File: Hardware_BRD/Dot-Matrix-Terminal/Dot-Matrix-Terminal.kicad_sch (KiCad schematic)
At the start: 61 parts, among them J1 USB_B, J2 Conn_01x17, J3 Conn_01x10, J4 Conn_01x02, J5 Barrel_Jack, J6 Conn_01x02, J7 Conn_01x02, J8 Conn_01x02, Q1 IRLML0030, Q10 IRLML0030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

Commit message: unsuccessful attempt at single layer routing
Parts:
- removed R22: 10k, Resistor_SMD:R_0603_1608Metric_Pad0.98x0.95mm_HandSolder, symbol Device:R
- added R23, R24, R25, R27: 10k, Resistor_SMD:R_0603_1608Metric_Pad0.98x0.95mm_HandSolder, symbol Device:R
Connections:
- net +24V: now also J7.1 (Pin_1), J7.2 (Pin_2); no longer J4.1 (Pin_1), J4.2 (Pin_2)
- net +3.3V: now also J4.1 (Pin_1), J4.2 (Pin_2), R15.2, R23.1, R24.2, R25.1, R27.1; no longer J7.1 (Pin_1), J7.2 (Pin_2), R15.1
- net FEED_L_SNS: now also U1.28 (IO17), R23.2; no longer U1.16 (IO13)
- net FEED_R: now also U1.24 (IO2); no longer Q11.1 (G), R11.1, U1.28 (IO17), U1.30 (IO18)
- net FEED_R_SNS: now also U1.30 (IO18), R24.1; no longer U1.13 (IO14)
- net FINE_SNS: now also R27.2
- net LINE_SNS: now also U1.27 (IO16), R25.2; no longer U1.14 (IO12)
- net PIN1: now also U1.16 (IO13); no longer U1.31 (IO19)
- net PIN3: now also U1.14 (IO12); no longer U1.24 (IO2)
- net PIN5: now also U1.13 (IO14); no longer U1.27 (IO16)
- net at Q15.3 (C), SW2.2, U1.25 (IO0): now also R15.1; no longer R15.2
- net INDEX_SNS: no longer names the net of J3.6 (Pin_6)
- net INDEX_SNS: no longer U1.23 (IO15)
- new net FEED_L: Q11.1 (G), R11.1, U1.23 (IO15)
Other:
- moved on the sheet: D1, D2, D3, D4, D5, D6, J4, J7, Q1, Q10, Q11, Q12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

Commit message: MVP board
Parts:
- removed R23, R24, R25, R27: 10k, Resistor_SMD:R_0603_1608Metric_Pad0.98x0.95mm_HandSolder, symbol Device:R
- added C7, C8: 1000u, Capacitor_THT:C_Radial_D16.0mm_H25.0mm_P7.50mm, symbol Device:C
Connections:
- net +24V: now also J6.1 (Pin_1), J6.2 (Pin_2), C7.1, C8.1; no longer J7.1 (Pin_1), J7.2 (Pin_2)
- net +3.3V: now also J8.1 (Pin_1), J8.2 (Pin_2); no longer J4.1 (Pin_1), J4.2 (Pin_2)
- net FEED_L: now also U1.26 (IO4); no longer U1.23 (IO15)
- net FEED_R: now also U1.27 (IO16); no longer U1.24 (IO2)
- net FINE_SNS: now also U1.28 (IO17); no longer U1.26 (IO4)
- net GND: now also J4.1 (Pin_1), J4.2 (Pin_2), J7.1 (Pin_1), J7.2 (Pin_2), C7.2, C8.2; no longer J6.1 (Pin_1), J6.2 (Pin_2), J8.1 (Pin_1), J8.2 (Pin_2)
- net LINE_SNS: now also U1.30 (IO18); no longer U1.27 (IO16)
- net MOTOR: now also U1.8 (IO32); no longer U1.6 (IO34)
- net PIN1: now also U1.24 (IO2); no longer U1.16 (IO13)
- net PIN2: now also U1.12 (IO27); no longer U1.10 (IO25)
- net PIN3: now also U1.23 (IO15); no longer U1.14 (IO12)
- net PIN4: now also U1.13 (IO14); no longer U1.11 (IO26)
- net PIN5: now also U1.16 (IO13); no longer U1.13 (IO14)
- net PIN6: now also U1.10 (IO25); no longer U1.8 (IO32)
- net PIN7: now also U1.14 (IO12); no longer U1.12 (IO27)
- net PIN8: now also U1.9 (IO33); no longer U1.7 (IO35)
- net PIN9: now also U1.11 (IO26); no longer U1.9 (IO33)
- net FEED_L_SNS: no longer names the net of J3.9 (Pin_9)
- net FEED_L_SNS: no longer U1.28 (IO17)
- net FEED_R_SNS: no longer names the net of J3.10 (Pin_10)
- net FEED_R_SNS: no longer U1.30 (IO18)
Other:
- moved on the sheet: J3, J4, J6, J7, J8, R13, R14

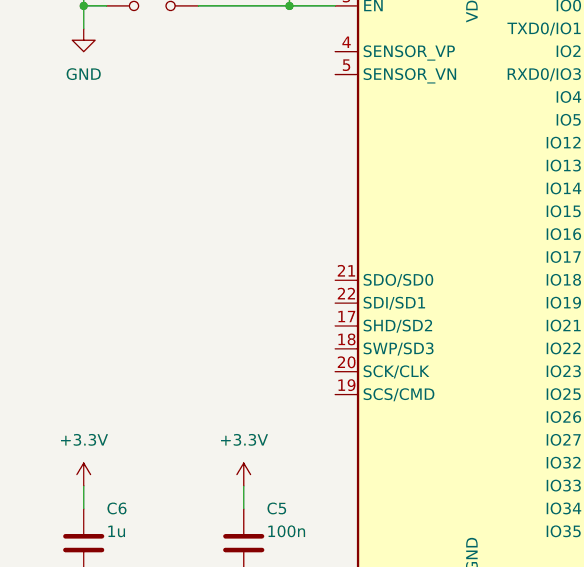
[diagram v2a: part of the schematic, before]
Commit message: Couple of mounting holes added
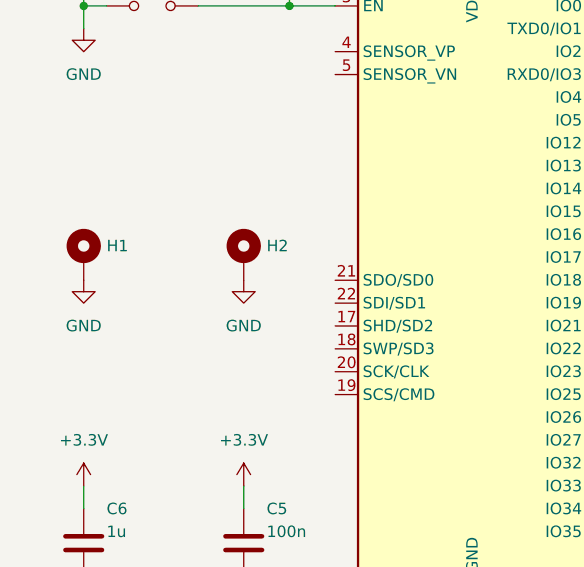
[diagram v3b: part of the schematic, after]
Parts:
- added H1, H2: MountingHole_Pad, MountingHole:MountingHole_3.2mm_M3_DIN965_Pad, symbol Mechanical:MountingHole_Pad
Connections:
- net GND: now also H1.1, H2.1
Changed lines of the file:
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@@
+    )
+  )
+  (symbol (lib_id "Mechanical:MountingHole_Pad") (at 43.18 99.06 0) (unit 1)
+    (in_bom yes) (on_board yes) (dnp no) (fields_autoplaced)
+    (property "Reference" "H2" (at 45.72 97.79 0)
+      (effects (font (size 1.27 1.27)) (justify left))
+    )
+    (property "Value" "MountingHole_Pad" (at 45.72 99.06 0)
+      (effects (font (size 1.27 1.27)) (justify left) hide)
+    )
+    (property "Footprint" "MountingHole:MountingHole_3.2mm_M3_DIN965_Pad" (at 43.18 99.06 0)
+      (effects (font (size 1.27 1.27)) hide)
+    )
+    (property "Datasheet" "~" (at 43.18 99.06 0)
+      (effects (font (size 1.27 1.27)) hide)
+    )
+    (pin "1")
+    (instances
+      (project "Dot-Matrix-Terminal"
+        (path "/3c4fbb2b-b39a-4597-9664-db9d6ef46a9c"
+          (reference "H2") (unit 1)
+        )
+      )
     )
   )
@@
         (path "/3c4fbb2b-b39a-4597-9664-db9d6ef46a9c"
           (reference "#PWR010") (unit 1)
+        )
+      )
+    )
+  )
+  (symbol (lib_id "power:GND") (at 25.4 101.6 0) (unit 1)
+    (in_bom yes) (on_board yes) (dnp no) (fields_autoplaced)
+    (property "Reference" "#PWR021" (at 25.4 107.95 0)
+      (effects (font (size 1.27 1.27)) hide)
+    )
+    (property "Value" "GND" (at 25.4 106.68 0)
+      (effects (font (size 1.27 1.27)))
+    )
+    (property "Footprint" "" (at 25.4 101.6 0)
+      (effects (font (size 1.27 1.27)) hide)
+    )
+    (property "Datasheet" "" (at 25.4 101.6 0)
+      (effects (font (size 1.27 1.27)) hide)
+    )
+    (pin "1")
+    (instances
+      (project "Dot-Matrix-Terminal"
+        (path "/3c4fbb2b-b39a-4597-9664-db9d6ef46a9c"
+          (reference "#PWR021") (unit 1)
         )
       )
@@
     )
   )
+  (symbol (lib_id "power:GND") (at 43.18 101.6 0) (unit 1)
+    (in_bom yes) (on_board yes) (dnp no) (fields_autoplaced)
+    (property "Reference" "#PWR030" (at 43.18 107.95 0)
+      (effects (font (size 1.27 1.27)) hide)
+    )
+    (property "Value" "GND" (at 43.18 106.68 0)
+      (effects (font (size 1.27 1.27)))
+    )
+    (property "Footprint" "" (at 43.18 101.6 0)
+      (effects (font (size 1.27 1.27)) hide)
+    )
+    (property "Datasheet" "" (at 43.18 101.6 0)
+      (effects (font (size 1.27 1.27)) hide)
+    )
+    (pin "1")
+    (instances
+      (project "Dot-Matrix-Terminal"
+        (path "/3c4fbb2b-b39a-4597-9664-db9d6ef46a9c"
+          (reference "#PWR030") (unit 1)
+        )
+      )
+    )
+  )
   (symbol (lib_id "Device:R") (at 128.27 109.22 270) (unit 1)
     (in_bom yes) (on_board yes) (dnp no)
@@
         )
       )
+    )
+  )
+  (symbol (lib_id "Mechanical:MountingHole_Pad") (at 25.4 99.06 0) (unit 1)
+    (in_bom yes) (on_board yes) (dnp no) (fields_autoplaced)
+    (property "Reference" "H1" (at 27.94 97.79 0)
+      (effects (font (size 1.27 1.27)) (justify left))
+    )
+    (property "Value" "MountingHole_Pad" (at 27.94 99.06 0)
+      (effects (font (size 1.27 1.27)) (justify left) hide)
+    )
+    (property "Footprint" "MountingHole:MountingHole_3.2mm_M3_DIN965_Pad" (at 25.4 99.06 0)
+      (effects (font (size 1.27 1.27)) hide)
+    )
+    (property "Datasheet" "~" (at 25.4 99.06 0)
+      (effects (font (size 1.27 1.27)) hide)
+    )
+    (pin "1")
+    (instances
+      (project "Dot-Matrix-Terminal"
+        (path "/3c4fbb2b-b39a-4597-9664-db9d6ef46a9c"
+          (reference "H1") (unit 1)
+        )
+      )
